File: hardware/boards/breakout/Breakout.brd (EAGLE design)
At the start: 42 x 42 mm, 4 parts

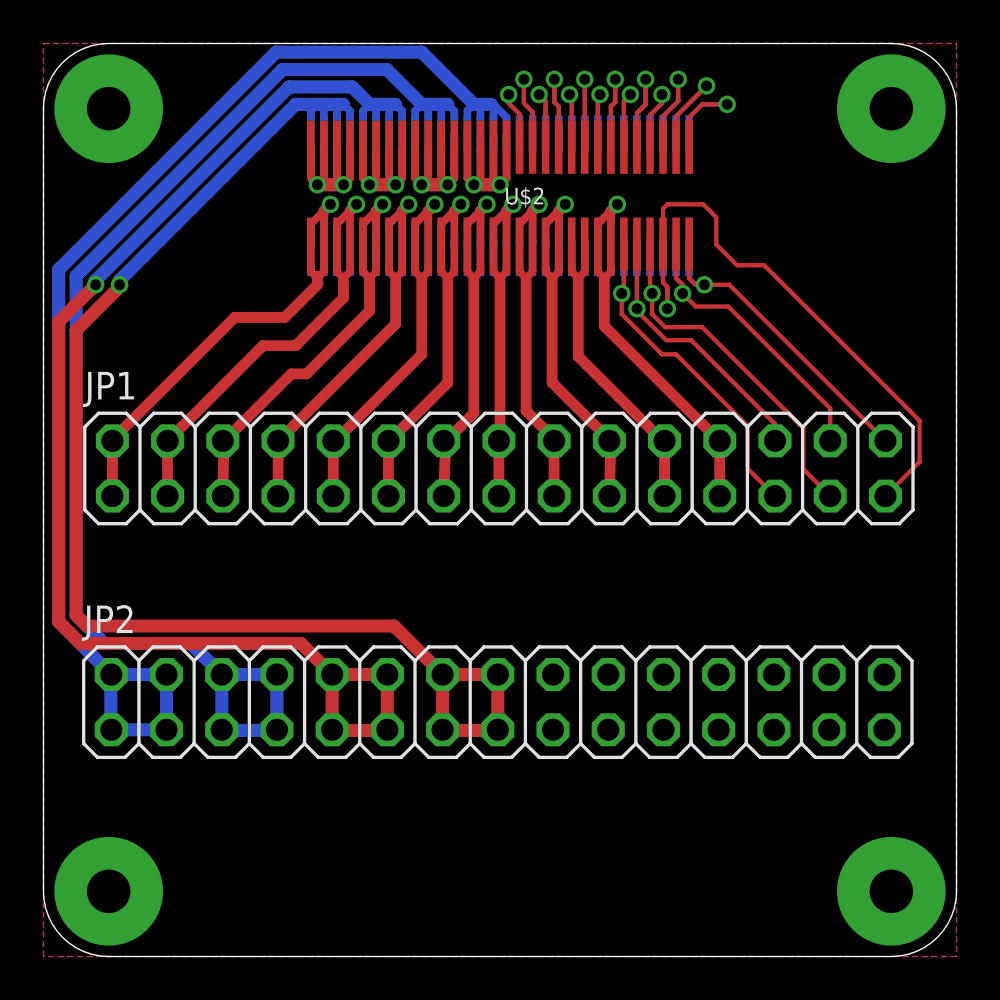
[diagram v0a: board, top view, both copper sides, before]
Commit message: completed routing breakout, need to tidy
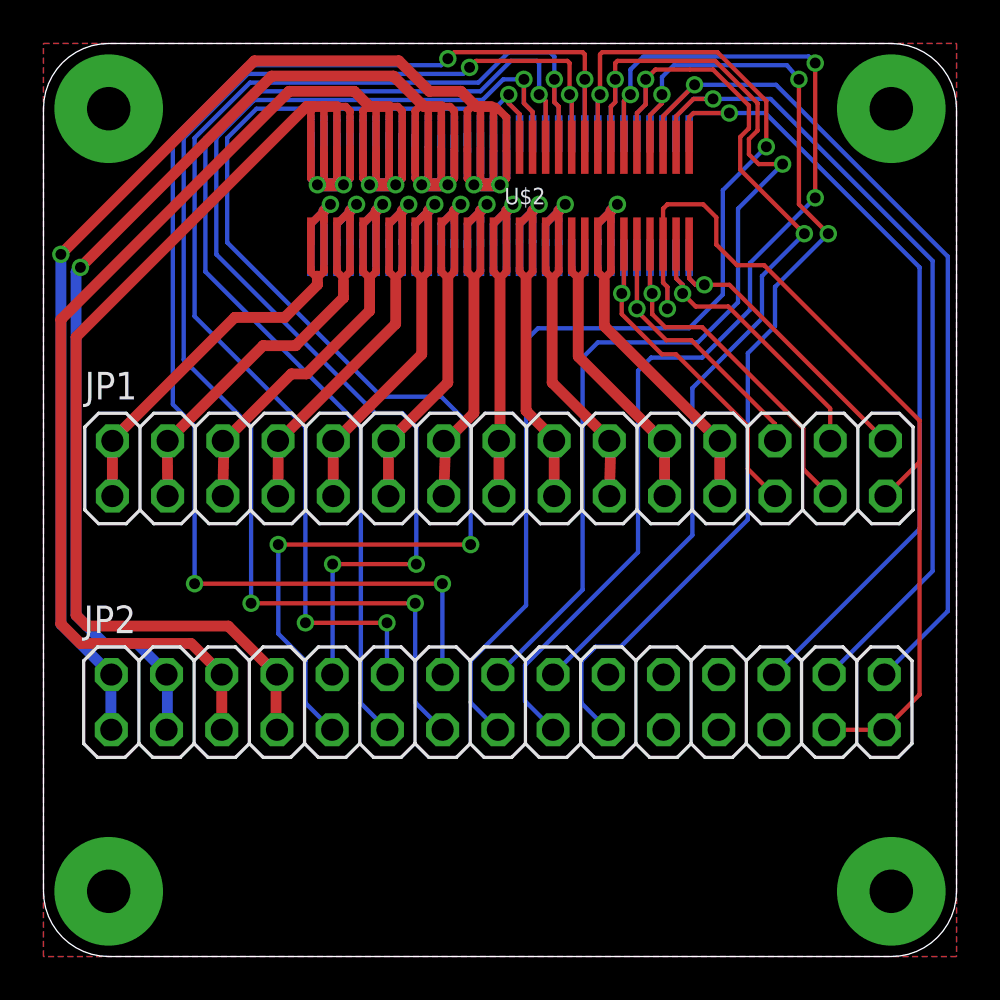
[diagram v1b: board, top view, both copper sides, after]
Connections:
- removed net N$31: JP2.17
- removed net N$32: JP2.19
- removed net N$36: JP2.27
- removed net N$37: JP2.29
- removed net N$38: JP2.30
- removed net N$39: JP2.28
- removed net N$40: JP2.26
- removed net N$44: JP2.18
- net +3V3_BUS: now also JP2.7, JP2.8; no longer JP2.13, JP2.14, JP2.15, JP2.16
- net /SS/GPIO2: now also JP2.19
- net BATV_BUS: now also JP2.3, JP2.4; no longer JP2.5, JP2.6, JP2.7, JP2.8
- net GND: now also JP2.27, JP2.29
- net GPIO10: now also JP2.11
- net GPIO11: now also JP2.10
- net GPIO12: now also JP2.9
- net GPIO3: now also JP2.18
- net GPIO4: now also JP2.17
- net GPIO5: now also JP2.16
- net GPIO6: now also JP2.15
- net GPIO7: now also JP2.14
- net GPIO8: now also JP2.13
- net GPIO9: now also JP2.12
- net MISO: now also JP2.28
- net MOSI: now also JP2.26
- net RTN_+3V3: now also JP2.5, JP2.6; no longer JP2.10, JP2.11, JP2.12, JP2.9
- net RTN_BATV: no longer JP2.3, JP2.4
- net SCK: now also JP2.30
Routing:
- net GPIO7: track 4.65 -> 62.9 mm, vias 1 -> 4
- net GPIO8: track 3.43 -> 60.7 mm, vias 1 -> 4
- net GPIO12: track 3.26 -> 60.4 mm, vias 1 -> 3
- net GPIO9: track 4.72 -> 54.6 mm, vias 1 -> 3
- net GPIO6: track 3.33 -> 52.9 mm, vias 1 -> 2
- net GPIO10: track 3.60 -> 52.5 mm
- net GPIO11: track 4.88 -> 53.2 mm, vias 1 -> 3
- net GPIO4: track 3.60 -> 51.7 mm, vias 1 -> 3
- net GPIO5: track 4.82 -> 48.8 mm, vias 1 -> 2
- net /SS/GPIO2: track 3.71 -> 47.7 mm, vias 1 -> 3
- net GPIO3: track 5.08 -> 43.0 mm, vias 1 -> 2
- net SCK: track 6.20 -> 41.7 mm
- net MISO: track 6.18 -> 40.5 mm
- net MOSI: track 6.12 -> 39.2 mm
- net +3V3_BUS: track 80.5 -> 64.4 mm, vias 3 -> 2
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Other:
- board text added: "Breakout Board"
- board text added: "SurreyEARS Pocketqube"
- board text added: "V0.1"

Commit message: Finished tidying traces for now.
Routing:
- net GPIO5: track 48.8 -> 46.9 mm
- net GPIO6: track 52.9 -> 51.1 mm
- net GPIO4: track 51.7 -> 50.3 mm
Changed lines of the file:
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@@
 <?xml version="1.0" encoding="utf-8"?>
 <!DOCTYPE eagle SYSTEM "eagle.dtd">
-<eagle version="7.2.0">
+<eagle version="7.0.0">
 <drawing>
 <settings>
@@
 <wire x1="32.9" y1="36.45" x2="34" y2="36.45" width="0.2" layer="1"/>
 <via x="34" y="36.45" extent="1-16" drill="0.5"/>
-<wire x1="34" y1="36.45" x2="31.95" y2="34.4" width="0.2" layer="16"/>
-<wire x1="31.95" y1="34.4" x2="31.95" y2="30.1" width="0.2" layer="16"/>
-<wire x1="31.95" y1="30.1" x2="30.1" y2="28.25" width="0.2" layer="16"/>
-<wire x1="30.1" y1="28.25" x2="25.5" y2="28.25" width="0.2" layer="16"/>
-<wire x1="25.5" y1="28.25" x2="24.8" y2="27.55" width="0.2" layer="16"/>
-<wire x1="24.8" y1="27.55" x2="24.8" y2="16.87" width="0.2" layer="16"/>
+<wire x1="34" y1="36.45" x2="31.5" y2="33.95" width="0.2" layer="16"/>
+<wire x1="31.5" y1="33.95" x2="31.5" y2="29.6" width="0.2" layer="16"/>
+<wire x1="31.5" y1="29.6" x2="26.85" y2="24.95" width="0.2" layer="16"/>
+<wire x1="26.85" y1="24.95" x2="25.45" y2="24.95" width="0.2" layer="16"/>
+<wire x1="25.45" y1="24.95" x2="24.8" y2="24.3" width="0.2" layer="16"/>
+<wire x1="24.8" y1="24.3" x2="24.8" y2="16.87" width="0.2" layer="16"/>
 <wire x1="24.8" y1="16.87" x2="20.9" y2="12.97" width="0.2" layer="16"/>
 <wire x1="26.1" y1="37.85" x2="26.1" y2="37.225" width="0" layer="19" extent="1-16"/>
@@
 <wire x1="32.5" y1="31.9" x2="32.5" y2="29.75" width="0.2" layer="16"/>
 <wire x1="32.5" y1="29.75" x2="30.3" y2="27.55" width="0.2" layer="16"/>
-<wire x1="30.3" y1="27.55" x2="27.95" y2="27.55" width="0.2" layer="16"/>
-<wire x1="27.95" y1="27.55" x2="27.35" y2="26.95" width="0.2" layer="16"/>
-<wire x1="27.35" y1="26.95" x2="27.35" y2="18.6" width="0.2" layer="16"/>
+<wire x1="30.3" y1="27.55" x2="27.95" y2="25.05" width="0.2" layer="16"/>
+<wire x1="27.95" y1="25.05" x2="27.35" y2="24.45" width="0.2" layer="16"/>
+<wire x1="27.35" y1="24.45" x2="27.35" y2="18.6" width="0.2" layer="16"/>
 <wire x1="27.35" y1="18.6" x2="22.15" y2="13.4" width="0.2" layer="16"/>
 <wire x1="22.15" y1="13.4" x2="22.15" y2="11.75" width="0.2" layer="16"/>
@@
 <via x="35" y="33.25" extent="1-16" drill="0.5"/>
 <wire x1="35" y1="33.25" x2="33.05" y2="31.3" width="0.2" layer="16"/>
-<wire x1="33.05" y1="31.3" x2="33.05" y2="29.35" width="0.2" layer="16"/>
-<wire x1="33.05" y1="29.35" x2="29.85" y2="26.15" width="0.2" layer="16"/>
-<wire x1="29.85" y1="26.15" x2="29.85" y2="19.38" width="0.2" layer="16"/>
+<wire x1="33.05" y1="31.3" x2="33.05" y2="29.45" width="0.2" layer="16"/>
+<wire x1="33.05" y1="29.45" x2="29.9" y2="26.25" width="0.2" layer="16"/>
+<wire x1="29.9" y1="26.25" x2="29.85" y2="19.38" width="0.2" layer="16"/>
 <wire x1="29.85" y1="19.38" x2="23.44" y2="12.97" width="0.2" layer="16"/>
 <wire x1="27.3" y1="37.85" x2="27.3" y2="37.225" width="0" layer="19" extent="1-16"/>
@@
 <via x="36.1" y="33.25" extent="1-16" drill="0.5"/>
 <wire x1="36.1" y1="33.25" x2="33.65" y2="30.8" width="0.2" layer="16"/>
-<wire x1="33.65" y1="30.8" x2="33.65" y2="29" width="0.2" layer="16"/>
-<wire x1="33.65" y1="29" x2="32.4" y2="27.75" width="0.2" layer="16"/>
-<wire x1="32.4" y1="27.75" x2="32.4" y2="20.1" width="0.2" layer="16"/>
+<wire x1="33.65" y1="30.8" x2="33.65" y2="29.25" width="0.2" layer="16"/>
+<wire x1="33.65" y1="29.25" x2="32.4" y2="28" width="0.2" layer="16"/>
+<wire x1="32.4" y1="28" x2="32.4" y2="20.1" width="0.2" layer="16"/>
 <wire x1="32.4" y1="20.1" x2="26.55" y2="14.25" width="0.2" layer="16"/>
 <wire x1="26.55" y1="14.25" x2="25.4" y2="14.25" width="0.2" layer="16"/>
@@
 <wire x1="33.25" y1="39.35" x2="33.25" y2="37.25" width="0.2" layer="1"/>
 <via x="33.25" y="37.25" extent="1-16" drill="0.5"/>
-<wire x1="33.25" y1="37.25" x2="31.25" y2="35.25" width="0.2" layer="16"/>
-<wire x1="31.25" y1="35.25" x2="31.25" y2="30.45" width="0.2" layer="16"/>
-<wire x1="31.25" y1="30.45" x2="29.7" y2="28.9" width="0.2" layer="16"/>
-<wire x1="29.7" y1="28.9" x2="22.75" y2="28.9" width="0.2" layer="16"/>
-<wire x1="22.75" y1="28.9" x2="22.2" y2="28.35" width="0.2" layer="16"/>
-<wire x1="22.2" y1="28.35" x2="22.2" y2="16.15" width="0.2" layer="16"/>
+<wire x1="33.25" y1="37.25" x2="31.05" y2="35.05" width="0.2" layer="16"/>
+<wire x1="31.05" y1="35.05" x2="31.05" y2="30.05" width="0.2" layer="16"/>
+<wire x1="31.05" y1="30.05" x2="26.6" y2="25.6" width="0.2" layer="16"/>
+<wire x1="26.6" y1="25.6" x2="22.75" y2="25.6" width="0.2" layer="16"/>
+<wire x1="22.75" y1="25.6" x2="22.2" y2="25.05" width="0.2" layer="16"/>
+<wire x1="22.2" y1="25.05" x2="22.2" y2="16.15" width="0.2" layer="16"/>
 <wire x1="22.2" y1="16.15" x2="19.65" y2="13.6" width="0.2" layer="16"/>
 <wire x1="19.65" y1="13.6" x2="19.65" y2="11.68" width="0.2" layer="16"/>
